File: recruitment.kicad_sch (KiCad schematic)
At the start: 3 parts, among them K1 Relay_SPST-NO, U1 ACS781xLRTR-050B

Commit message: partial wiring and monitor draft
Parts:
- added BT1: 5, symbol Device:Battery_Cell
- added D2, D3: LED, LED_THT:LED_D3.0mm, symbol Device:LED
- added R3, R4: R, symbol Device:R
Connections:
- net Monitor/SENS: now reaches U1.3 (VOUT)
- net 24-48V: now reaches K1.14
- net Monitor/M_A1V: now reaches K1.A1
- net Monitor/M_A2V: now reaches K1.A2
- net 9-17V: now reaches V1.1
- net 9-17V: now also R3.2
- net GND: now reaches V1.2
- net GND: now also D2.1 (K), D3.1 (K)
- new net: D2.2 (A), R3.1
- new net: D3.2 (A), R4.1
- new net Monitor/M_VIN: BT1.1 (+), R4.2
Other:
- sheet Boost Converter ports: added V_BSTD; removed none
- sheet Monitor ports: added M_A1V, M_A2V, M_GND, M_VIN, SENS; removed none
- moved on the sheet: K1, U1, V1

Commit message: monitor changes
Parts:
- added RL: R, symbol Device:R
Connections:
- net GND: now also U1.2 (GND), U1.6 (IP-), RL.2
- net Monitor/M_VIN: now also U1.1 (VCC)
- net at U1.5 (IP+): now also K1.13, RL.1
- no-connect marks 0 -> 2
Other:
- moved on the sheet: U1

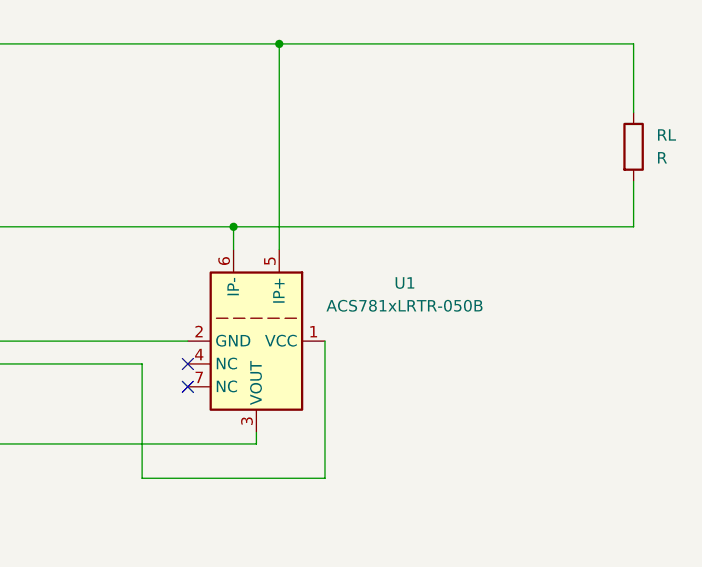
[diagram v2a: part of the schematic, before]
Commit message: monitor internals: temporary solution
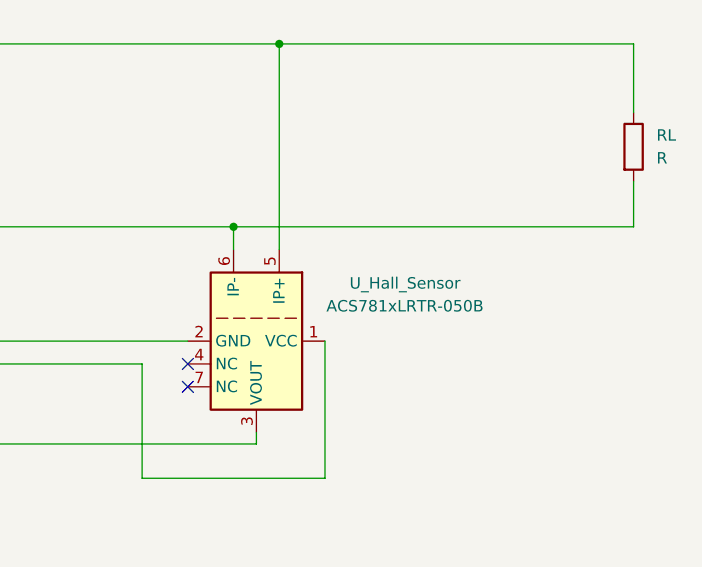
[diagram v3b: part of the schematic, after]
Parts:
- renumbered U1 to U_Hall_Sensor
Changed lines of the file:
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@@
 		(dnp no)
 		(fields_autoplaced yes)
-		(property "Reference" "U1"
+		(property "Reference" "U_Hall_Sensor"
 			(at 177.8 68.5098 90)
 			(effects
@@
 			(project ""
 				(path "/bdc7face-9f7c-4701-80bb-4cc144448db1"
-					(reference "U1")
+					(reference "U_Hall_Sensor")
 					(unit 1)
 				)

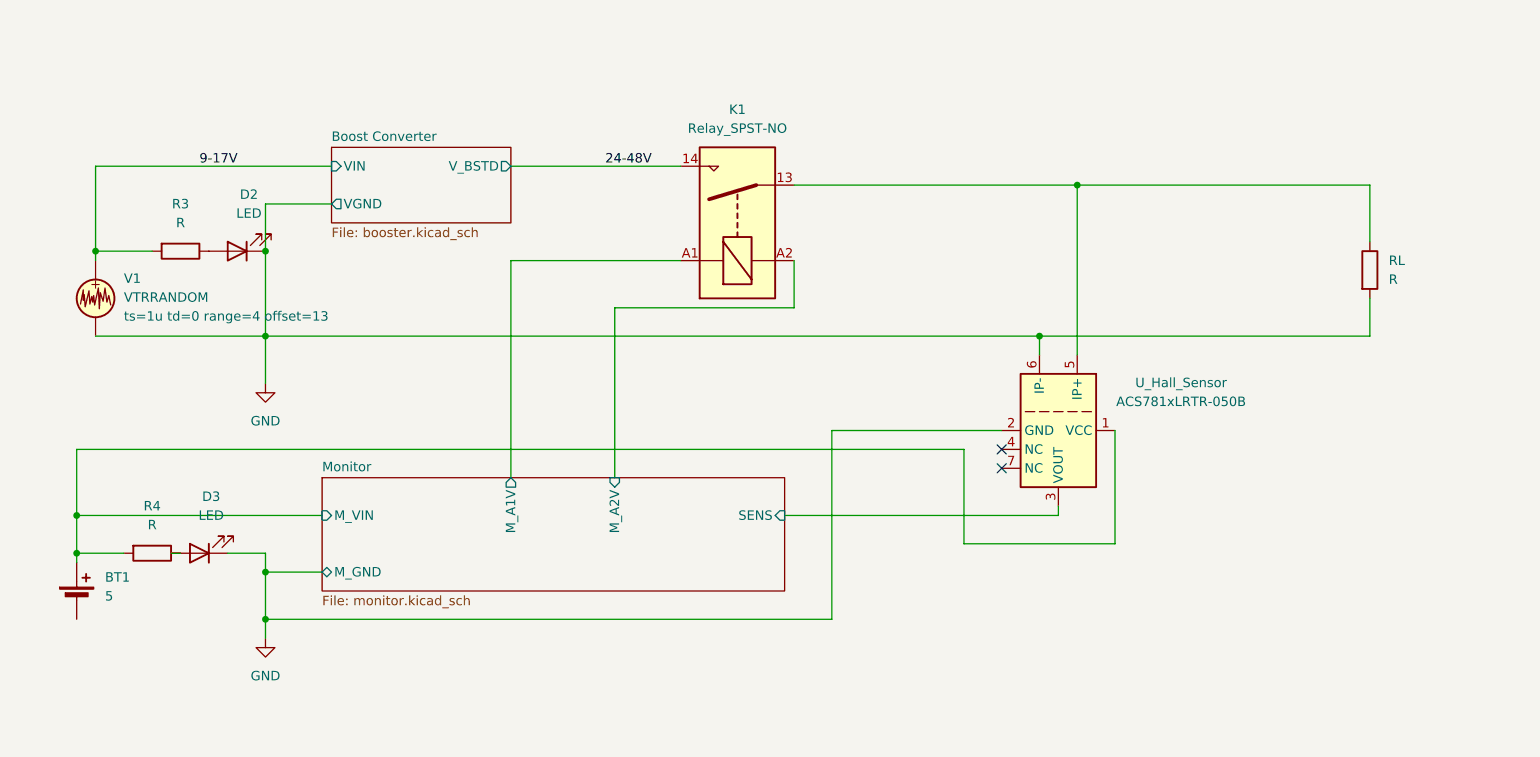
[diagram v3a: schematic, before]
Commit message: corrected monitor source
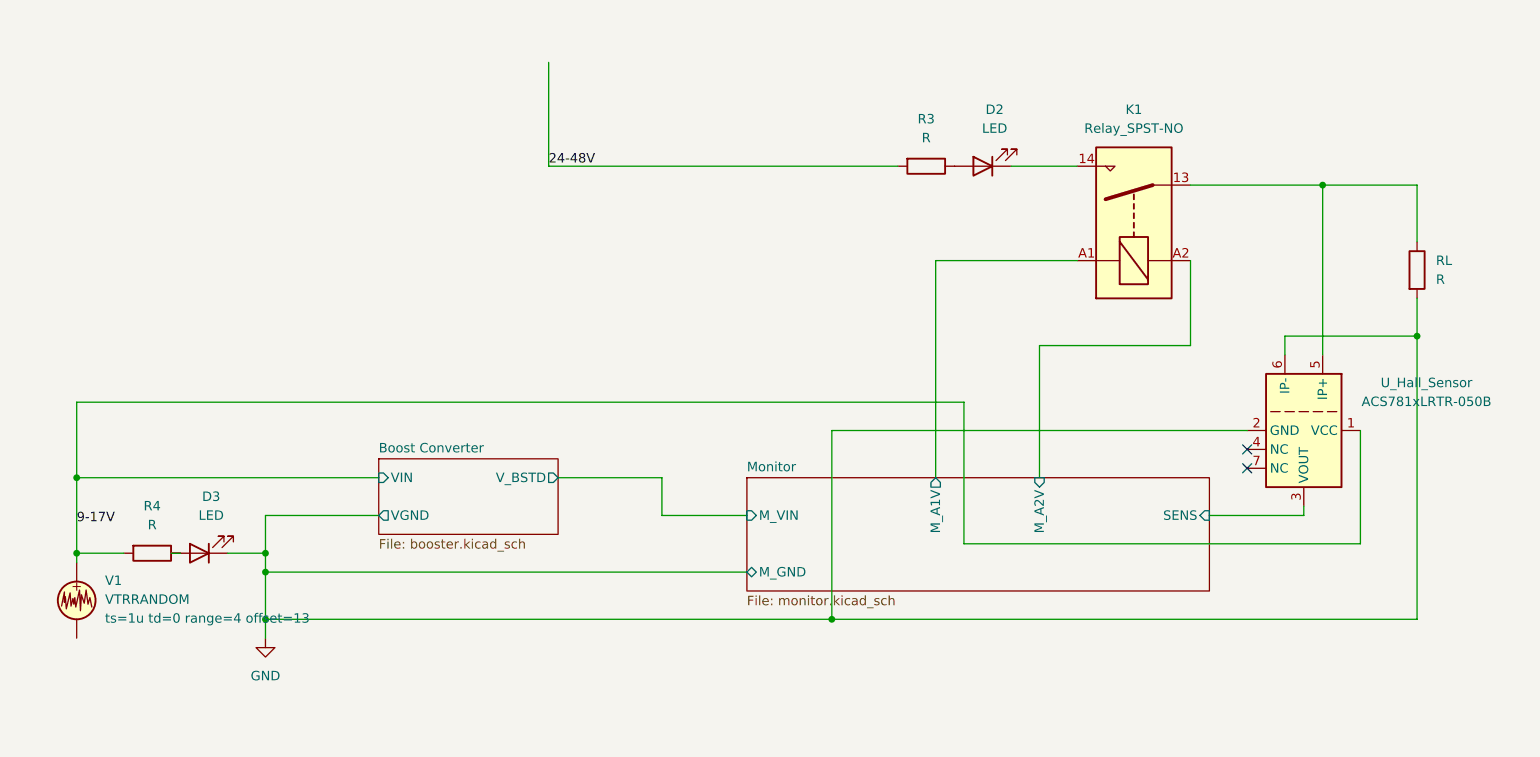
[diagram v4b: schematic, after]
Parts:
- removed BT1: 5, symbol Device:Battery_Cell
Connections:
- net Monitor/M_VIN is gone; now on net 9-17V: R4.2, U_Hall_Sensor.1 (VCC)
- net 24-48V: now also R3.2; no longer K1.14
- net 9-17V: no longer R3.2
- net GND: no longer D2.1 (K), V1.2
- new net: D2.1 (K), K1.14
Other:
- moved on the sheet: D2, K1, R3, RL, U_Hall_Sensor, V1

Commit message: added LPF and correct load LED
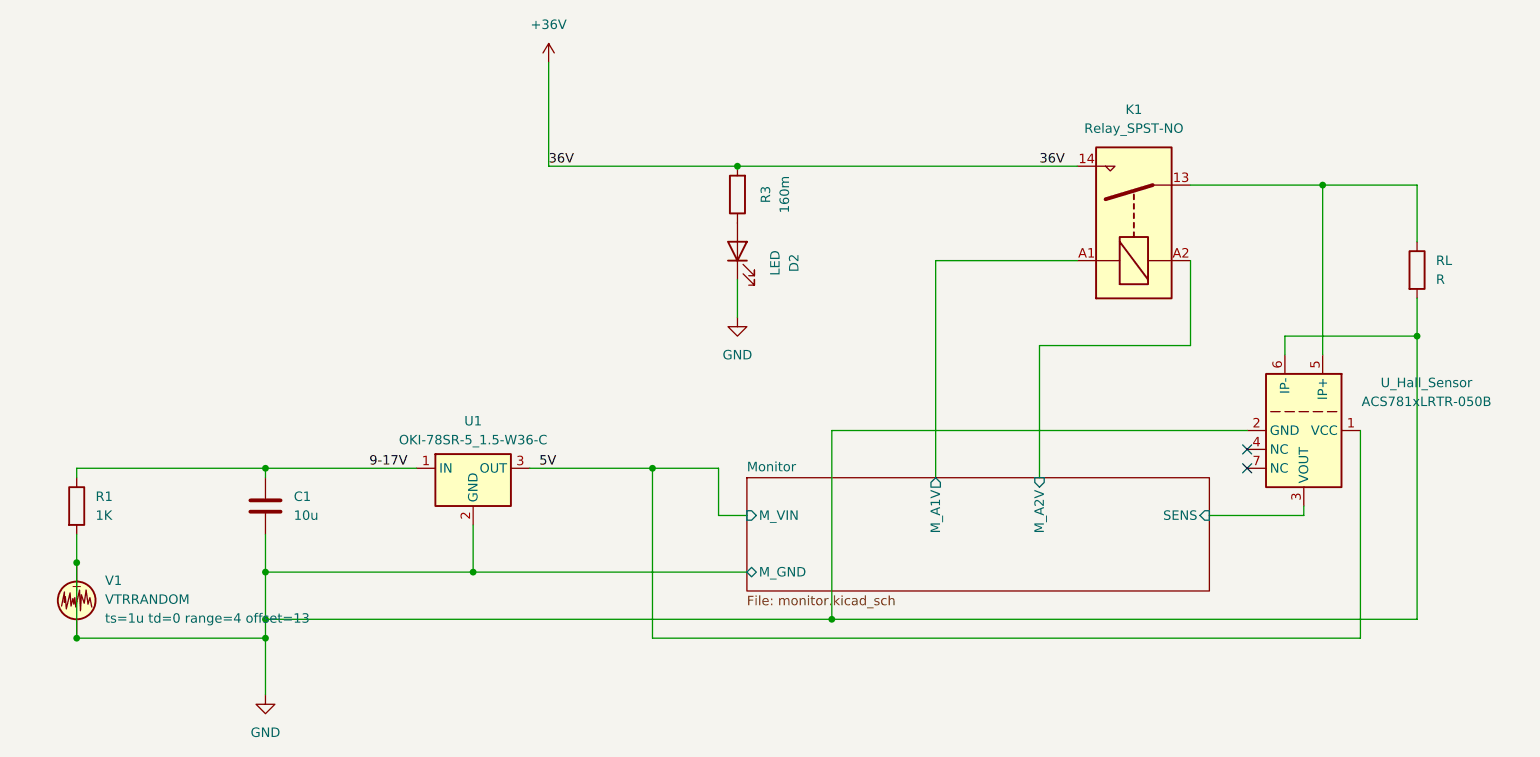
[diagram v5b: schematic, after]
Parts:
- removed D3: LED, LED_THT:LED_D3.0mm, symbol Device:LED
- removed R4: R, symbol Device:R
- added C1: 10u, symbol Device:C
- added R1: 1K, symbol Device:R
- added U1: OKI-78SR-5_1.5-W36-C, Converter_DCDC:Converter_DCDC_Murata_OKI-78SR_Vertical, symbol Converter_DCDC:OKI-78SR-5_1.5-W36-C
- R3: value R -> 160m
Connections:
- net 24-48V is gone; now on net +36V: R3.2
- net 9-17V: now also C1.1, R1.1, U1.1 (IN); no longer U_Hall_Sensor.1 (VCC), V1.1
- net GND: now also D2.1 (K), V1.1, V1.2, C1.2, R1.2, U1.2 (GND)
- net +36V: now reaches K1.14
- net +36V: no longer D2.1 (K)
- new net 5V: U1.3 (OUT), U_Hall_Sensor.1 (VCC)
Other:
- removed sheet Boost Converter
- moved on the sheet: D2, R3

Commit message: calculated resistances and corrected LPF
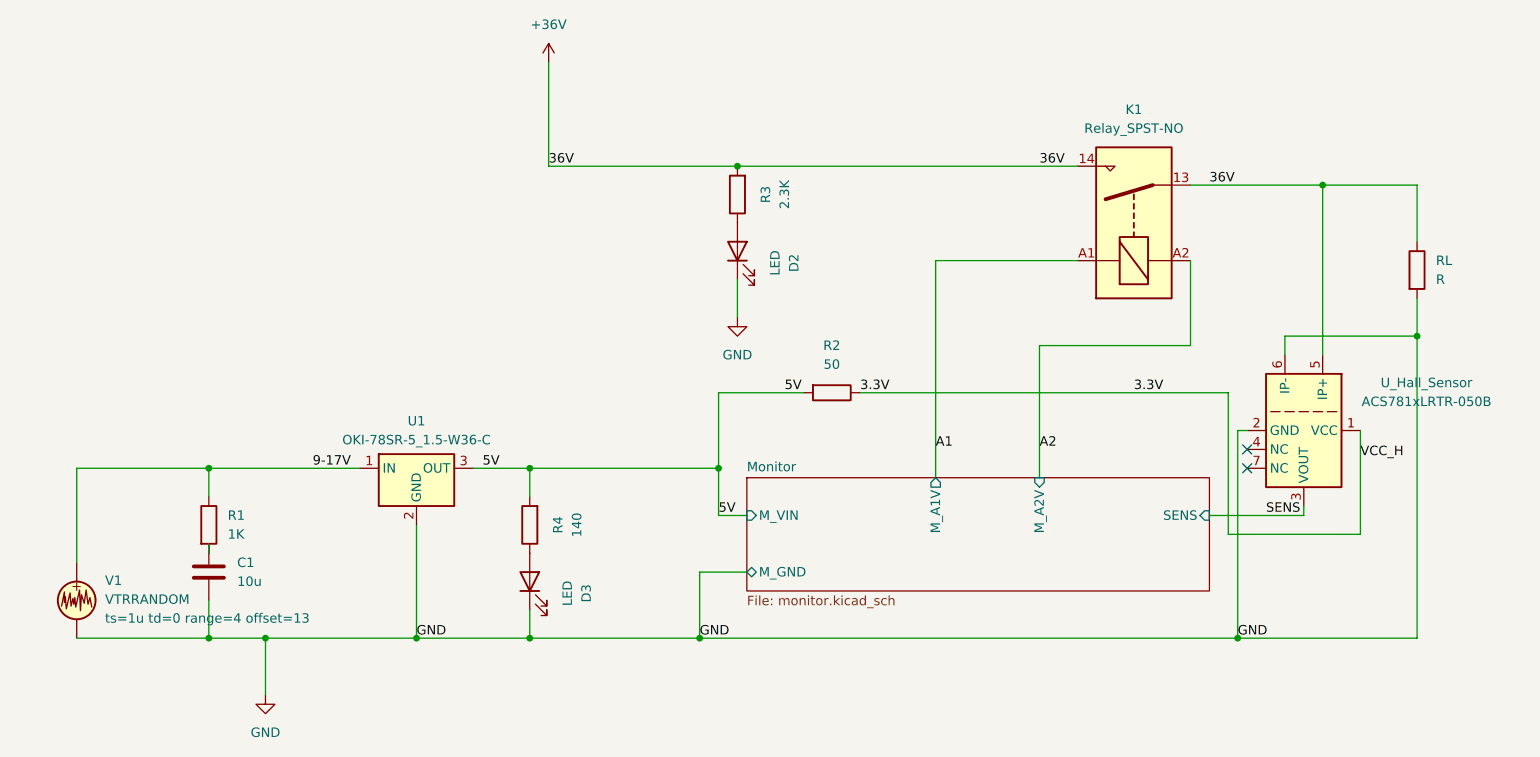
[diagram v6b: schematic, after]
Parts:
- added D3: LED, LED_THT:LED_D3.0mm, symbol Device:LED
- added R2: 50, symbol Device:R
- added R4: 140, symbol Device:R
- R3: value 160m -> 2.3K
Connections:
- net +36V: now also K1.13, RL.1, U_Hall_Sensor.5 (IP+)
- net 5V: now also R2.2, R4.2; no longer U_Hall_Sensor.1 (VCC)
- net 9-17V: now also V1.1; no longer C1.1
- net GND: now also D3.1 (K); no longer R1.2, V1.1
- net Monitor/M_A1V renamed A1
- net Monitor/M_A2V renamed A2
- net Monitor/SENS renamed SENS
- new net: C1.1, R1.2
- new net: D3.2 (A), R4.1
- new net 3.3V: R2.1, U_Hall_Sensor.1 (VCC)
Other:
- moved on the sheet: C1, R1, U1
